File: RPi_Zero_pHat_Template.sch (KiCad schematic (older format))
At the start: 2 parts, among them J1 RPi_GPIO, J2 RPi_GPIO

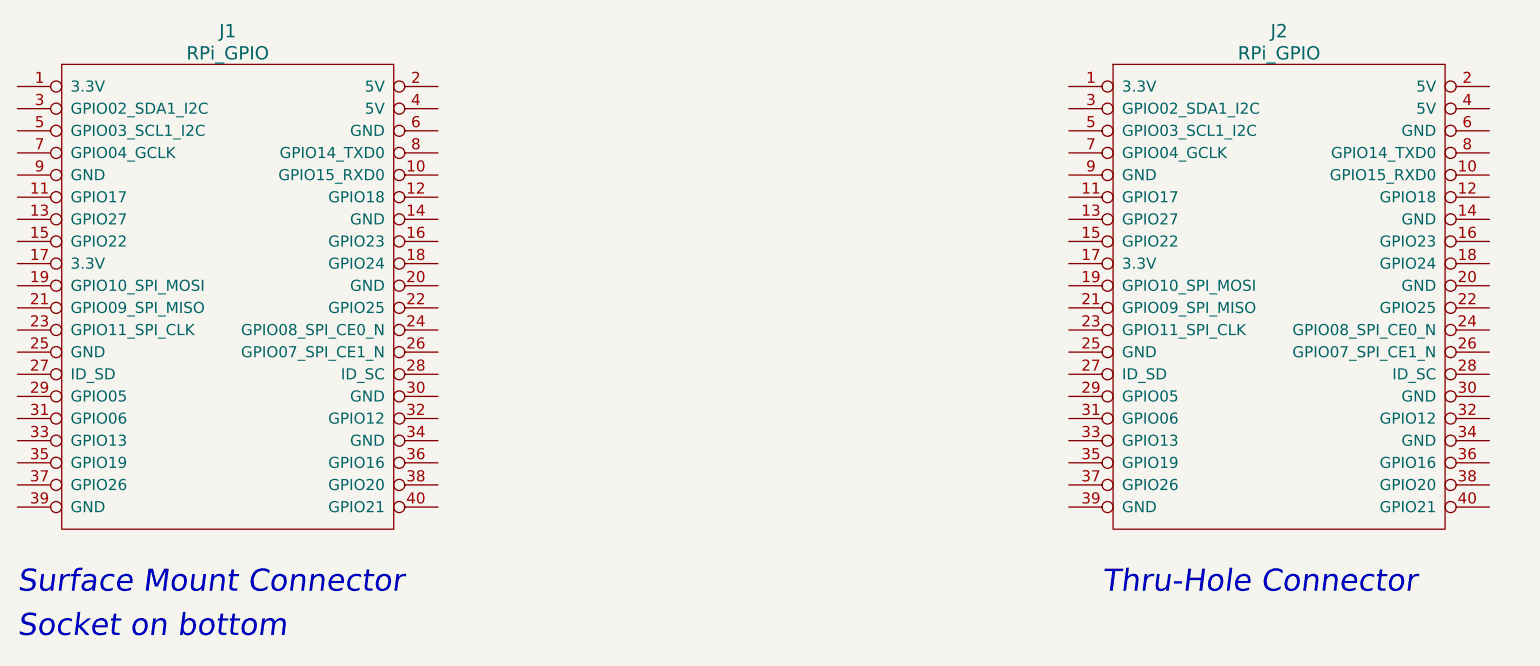
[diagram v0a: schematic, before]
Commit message: Schematic: Removed the surface-mount header
Since we'll be sticking with through-hole.
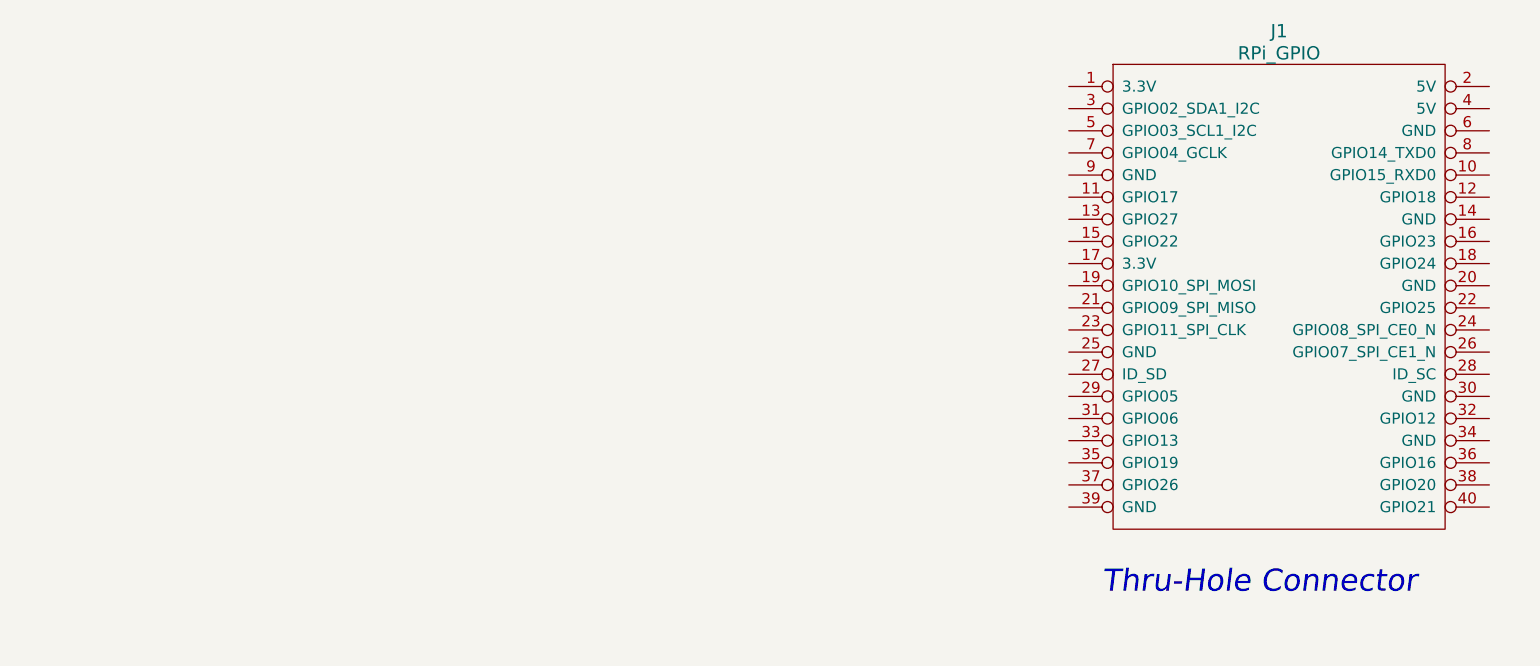
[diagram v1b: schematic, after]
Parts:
- removed J1: RPi_GPIO, RPi_Hat:Samtec_HLE-120-02-XXX-DV-BE-XX-XX, symbol Connector-ML:RPi_GPIO
- renumbered J2 to J1
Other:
- note removed: "Socket on bottom"
- note removed: "Surface Mount Connector"
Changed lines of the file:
@@
 EESchema Schematic File Version 4
-LIBS:RPi_Zero_pHat_Template-cache
-EELAYER 26 0
+EELAYER 30 0
 EELAYER END
 $Descr A4 11693 8268
@@
 $Comp
 L Connector-ML:RPi_GPIO J1
-U 1 1 5515D39E
-P 2750 2700
-F 0 "J1" H 3500 2950 60  0000 C CNN
-F 1 "RPi_GPIO" H 3500 2850 60  0000 C CNN
-F 2 "RPi_Hat:Samtec_HLE-120-02-XXX-DV-BE-XX-XX" H 2750 2700 60  0001 C CNN
-F 3 "" H 2750 2700 60  0000 C CNN
-	1    2750 2700
-	1    0    0    -1
-$EndComp
-$Comp
-L Connector-ML:RPi_GPIO J2
 U 1 1 5516AE26
 P 7500 2700
-F 0 "J2" H 8250 2950 60  0000 C CNN
+F 0 "J1" H 8250 2950 60  0000 C CNN
 F 1 "RPi_GPIO" H 8250 2850 60  0000 C CNN
 F 2 "RPi_Hat:Pin_Header_Straight_2x20" H 7500 2700 60  0001 C CNN
@@
 	1    0    0    -1
 $EndComp
-Text Notes 2550 5000 0    100  Italic 0
-Surface Mount Connector
 Text Notes 7450 5000 0    100  Italic 0
 Thru-Hole Connector
-Text Notes 2550 5200 0    100  Italic 0
-Socket on bottom
 $EndSCHEMATC

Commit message: Schematic: Fixed the footprint selection for the through-hole
Seemed to be trying to use something that didn't exist... It should now be using
the footprint that the original PCB was using.
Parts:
- J1: footprint RPi_Hat:Pin_Header_Straight_2x20 -> Connector_PinHeader_2.54mm:PinHeader_2x20_P2.54mm_Vertical
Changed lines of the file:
@@
 F 0 "J1" H 8250 2950 60  0000 C CNN
 F 1 "RPi_GPIO" H 8250 2850 60  0000 C CNN
-F 2 "RPi_Hat:Pin_Header_Straight_2x20" H 7500 2700 60  0001 C CNN
+F 2 "Connector_PinHeader_2.54mm:PinHeader_2x20_P2.54mm_Vertical" H 7500 2700 60  0001 C CNN
 F 3 "" H 7500 2700 60  0000 C CNN
 	1    7500 2700
